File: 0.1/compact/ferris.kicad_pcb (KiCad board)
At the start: 2 copper layers, 208.7 x 86.7 mm, 102 parts, among them J1 USB C, K0_0 KEYSW, K0_1 KEYSW, K0_2 KEYSW, K0_3 KEYSW, K0_4 KEYSW, K0_5 KEYSW, K0_6 KEYSW, K0_7 KEYSW, K0_8 KEYSW, K0_9 KEYSW, K1_0 KEYSW, K1_1 KEYSW, K1_2 KEYSW, K1_3 KEYSW, K1_4 KEYSW, K1_5 KEYSW, K1_6 KEYSW, K1_7 KEYSW, K1_8 KEYSW, K1_9 KEYSW, K2_0 KEYSW, K2_1 KEYSW, K2_2 KEYSW, K2_3 KEYSW, K2_4 KEYSW, K2_5 KEYSW, K2_6 KEYSW, K2_8 KEYSW, K2_9 KEYSW, K3_3 KEYSW, K3_4 KEYSW, K3_5 KEYSW, K3_6 KEYSW, SW1 Reset, U1 ATmega32U4-AU, U2 MCP23017_SO, Y1 Crystal

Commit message: 0.1/compact: Use my own footprints where appropriate
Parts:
- removed the mouse-bite-2mm-slot at (103.2, 38.5)
- removed the mouse-bite-2mm-slot at (132.8, 38.5)
- added mouse-bite-2mm-slot: VAL**, panelization:mouse-bite-2mm-slot, F.Cu at (103.2, 38.5)
- added mouse-bite-2mm-slot: VAL**, panelization:mouse-bite-2mm-slot, F.Cu at (132.8, 38.5)
- G***: footprint ferris:unsafe_rust -> silkscreens:unsafe_rust
- G***: footprint ferris:safe_rust -> silkscreens:safe_rust
- G*** (x2): footprint ferris:ferris_compact_pad -> copper_pads:ferris_compact
- mouse-bite-2mm-slot: footprint Panelization:mouse-bite-2mm-slot -> panelization:mouse-bite-2mm-slot

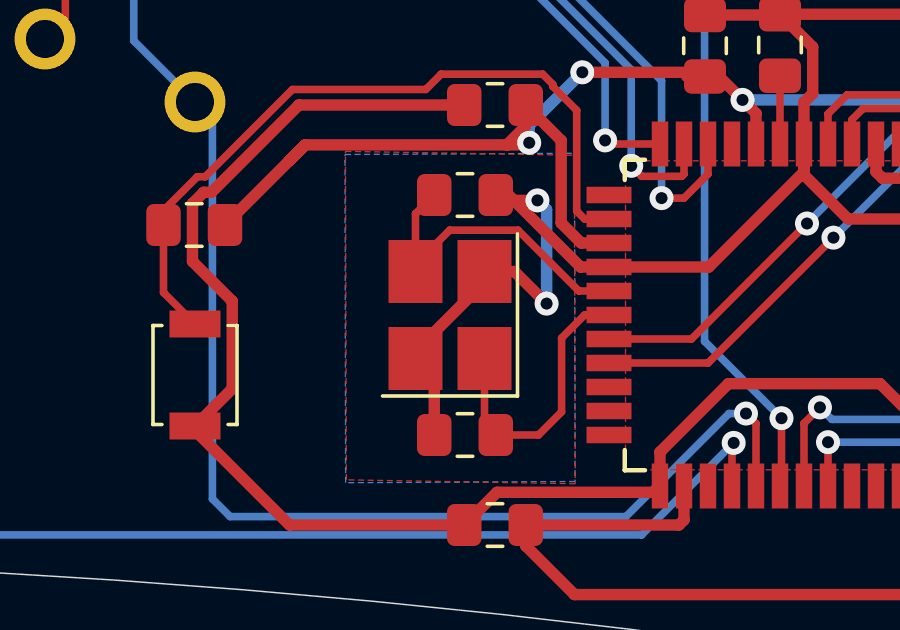
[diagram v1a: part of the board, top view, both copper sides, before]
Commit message: 0.1/compact: update footprints from schematic
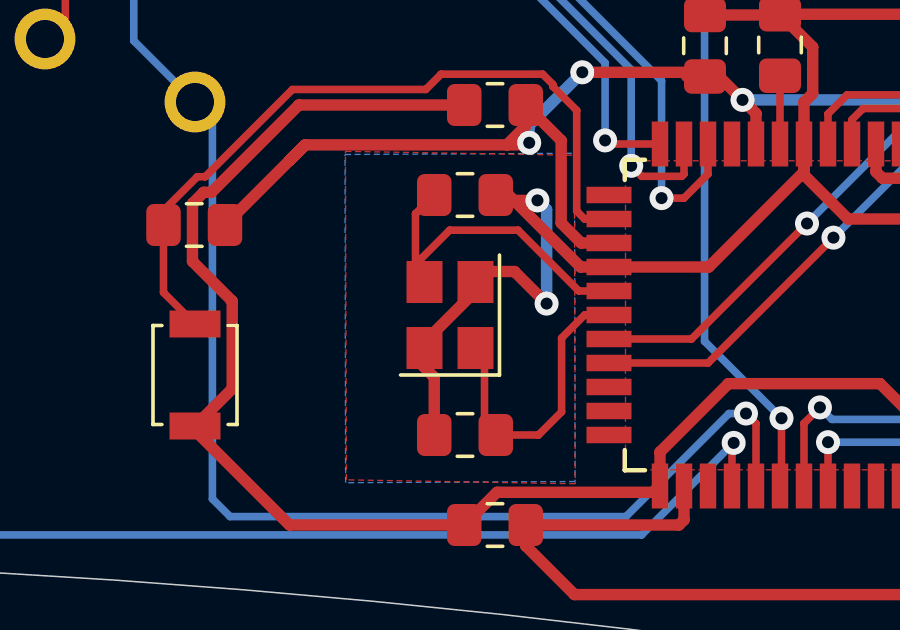
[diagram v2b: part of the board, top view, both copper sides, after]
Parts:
- C1, C2: value 22pF -> 22p
- C10, C3, C4, C5, C6, C9: value 0.1uF -> 0.1u
- C7: value 4.7uF -> 4.7u
- C8: value 1uF -> 1u
- K0_0, K0_1, K0_2, K0_3, K0_4, K0_5, K0_6, K0_7, K0_8, K0_9, K1_0, K1_1, K1_2, K1_3, K1_4, K1_5, K1_6, K1_7, K1_8, K1_9, K2_0, K2_1, K2_2, K2_3, K2_4, K2_5, K2_6, K2_8, K2_9, K3_3, K3_4, K3_5, K3_6: footprint ferris:SW_PG1350_choc_spacing -> switches:Choc_PG1350_Choc_Spacing
- K2_7: renamed from K; footprint ferris:SW_PG1350_choc_spacing -> switches:Choc_PG1350_Choc_Spacing
- R1, R2, R9: value 10kΩ -> 10k
- R3, R4: value 22Ω -> 22
- R5, R6: value 5.1KΩ -> 5.1K
- R7, R8: value 4.7kΩ -> 4.7k
- SW1: value Reset -> SW_PUSH
- Y1: footprint Crystal:Crystal_SMD_3225-4Pin_3.2x2.5mm_HandSoldering -> Crystal:Crystal_SMD_3225-4Pin_3.2x2.5mm
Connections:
- J1 pad S1: GND -> Net-(J1-PadS1)
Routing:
- net Net-(J1-PadS1): track 0.00 -> 17.0 mm
- net GND: track 215.7 -> 198.7 mm
